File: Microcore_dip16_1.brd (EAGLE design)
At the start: 68.7 x 27.9 mm, 17 parts, among them IC1 74LS595N, IC2 7459716DIP

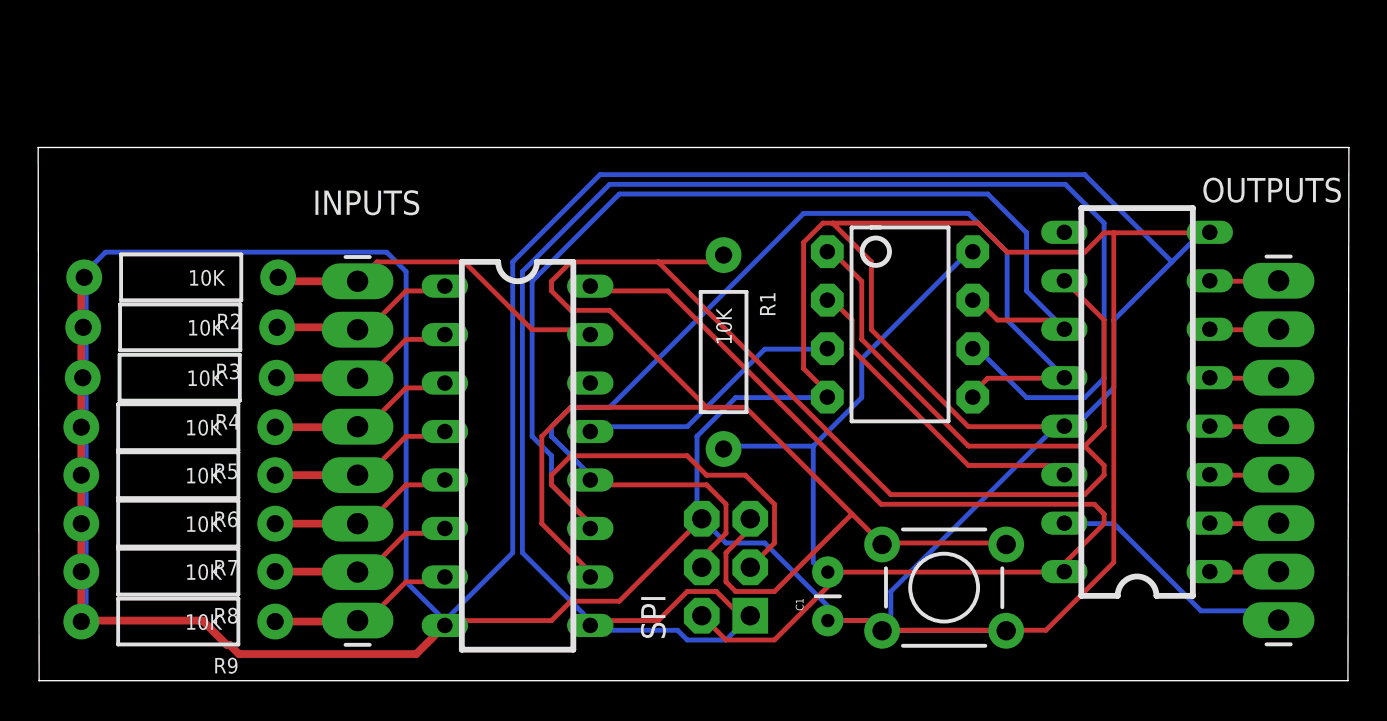
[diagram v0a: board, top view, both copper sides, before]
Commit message: Added resistor array and power regulator
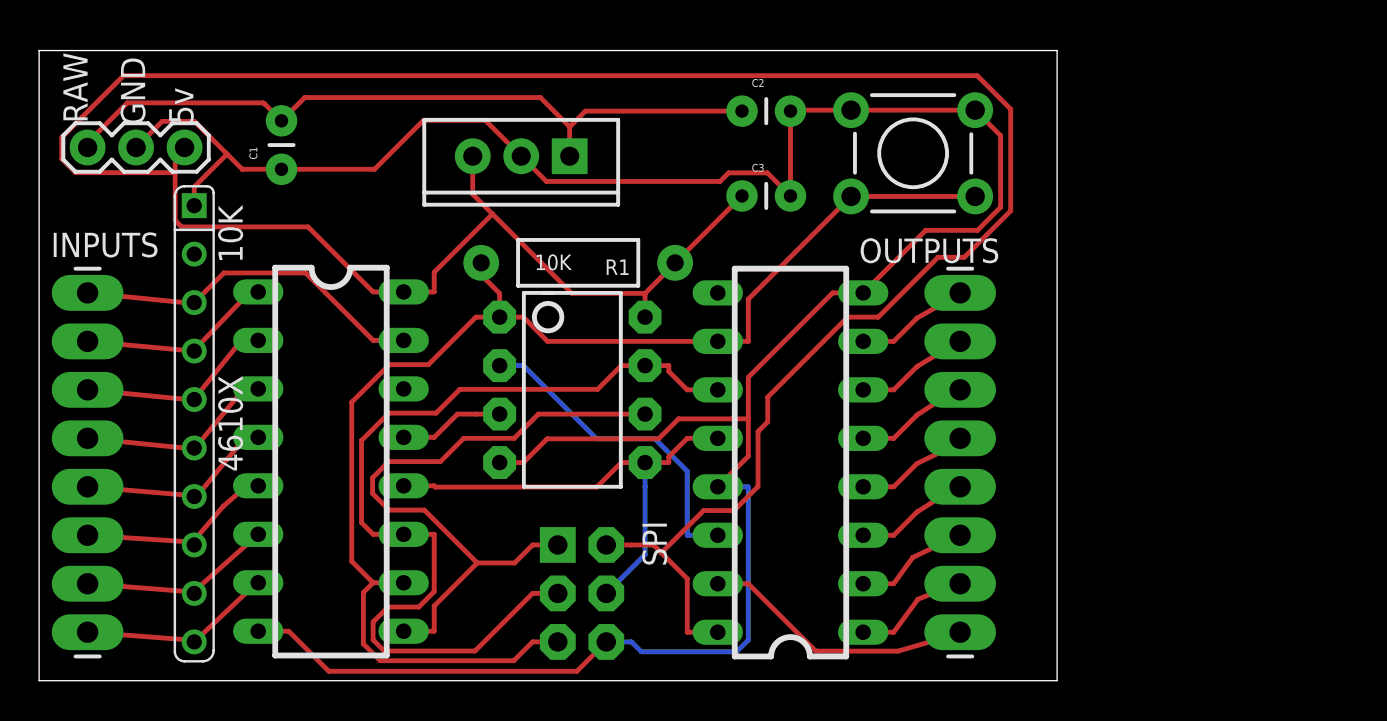
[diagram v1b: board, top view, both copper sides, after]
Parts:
- removed R2, R3, R4, R5, R6, R7, R8, R9: 10K, SparkFun:AXIAL-0.4
- added 10K: 4610X, Dustin:10-SIP
- added C2, C3: 22uf, SparkFun:CAP-PTH-SMALL
- added JP1: (no value), SparkFun:1X03
- added U$2: LM805, SparkFun:TO220-IGO
- IC1: value 74LS595N -> 74*595
- IC2: value 7459716DIP -> 74*597
- moved C1 37.1 mm to (12.7, 26.8)
- moved S1 22.8 mm to (45.8, 27.6), turned to 0 degrees
- moved IC1 18.4 mm to (39.4, 11.4)
- moved U$1 17.5 mm to (27.9, 15.2)
- moved OUTPUTS 16.7 mm to (48.3, 2.54)
- moved INPUTS 14.2 mm to (2.54, 20.3)
- moved IC2 9.78 mm to (15.3, 12.8)
- moved R1 8.94 mm to (28.2, 21.9), turned to 0 degrees
- moved SPI 7.67 mm to (28.4, 4.57), turned to 270 degrees
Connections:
- net OUTPUT renamed OUTPUT_SER
- net S_OUT renamed INPUT_SER
- new net RAW: C1.2, C2.1, JP1.1, U$2.IN
- net GND: now also 10K.P$1, C2.2, C3.2, JP1.2, U$2.GND; no longer R2.P$2, R3.P$2, R4.P$2, R5.P$2, R6.P$2, R7.P$2, R8.P$2, R9.P$2
- net N$10: now also 10K.P$4; no longer R3.P$1
- net N$11: now also 10K.P$5; no longer R4.P$1
- net N$12: now also 10K.P$6; no longer R5.P$1
- net N$13: now also 10K.P$7; no longer R6.P$1
- net N$14: now also 10K.P$8; no longer R7.P$1
- net N$15: now also 10K.P$9; no longer R8.P$1
- net N$16: now also 10K.P$10; no longer R9.P$1
- net N$9: now also 10K.P$3; no longer R2.P$1
- net VCC: now also C3.1, JP1.3, U$2.OUT; no longer C1.2
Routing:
- net GND: track 315.2 -> 136.7 mm
- net VCC: track 83.5 -> 148.2 mm
- net RESET: track 129.7 -> 68.6 mm
- net INPUT_SER: track 89.1 -> 34.2 mm
- net RAW: track 0.00 -> 38.8 mm
- net LATCH: track 57.9 -> 25.4 mm
- net SCK: track 74.8 -> 48.3 mm
- net LOAD: track 14.4 -> 5.53 mm
- net N$5: track 3.64 -> 6.15 mm
- net N$7: track 3.64 -> 6.12 mm
- net N$2: track 3.64 -> 6.11 mm
- net N$6: track 3.64 -> 6.06 mm
- net N$3: track 3.64 -> 6.05 mm
- net N$4: track 3.64 -> 6.03 mm
- net N$8: track 3.64 -> 5.95 mm
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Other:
- board size 68.7 x 27.9 mm -> 53.3 x 33 mm
- board text added: "5v"
- board text added: "GND"
- board text added: "RAW"
